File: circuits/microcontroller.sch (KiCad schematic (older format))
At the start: 18 parts, among them J2 Conn_02x07_Odd_Even, SW2 SW_PUSH, SW3 SW_PUSH, SW4 SW_PUSH, U3 ESP-WROOM-32, U4 SI7020-A20

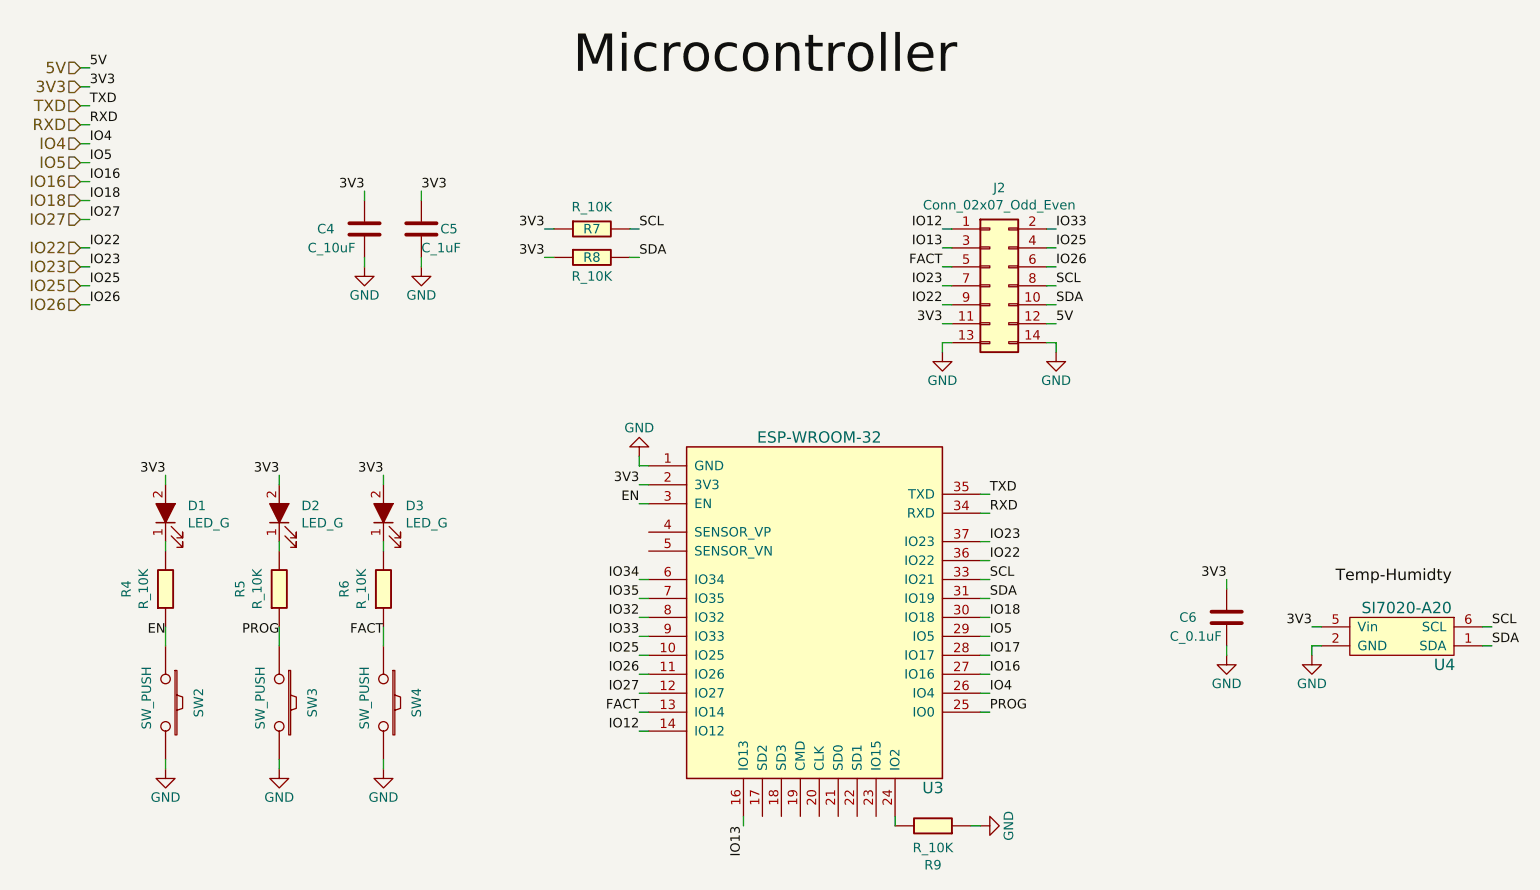
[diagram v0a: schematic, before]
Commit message: sending new board to boardhouse
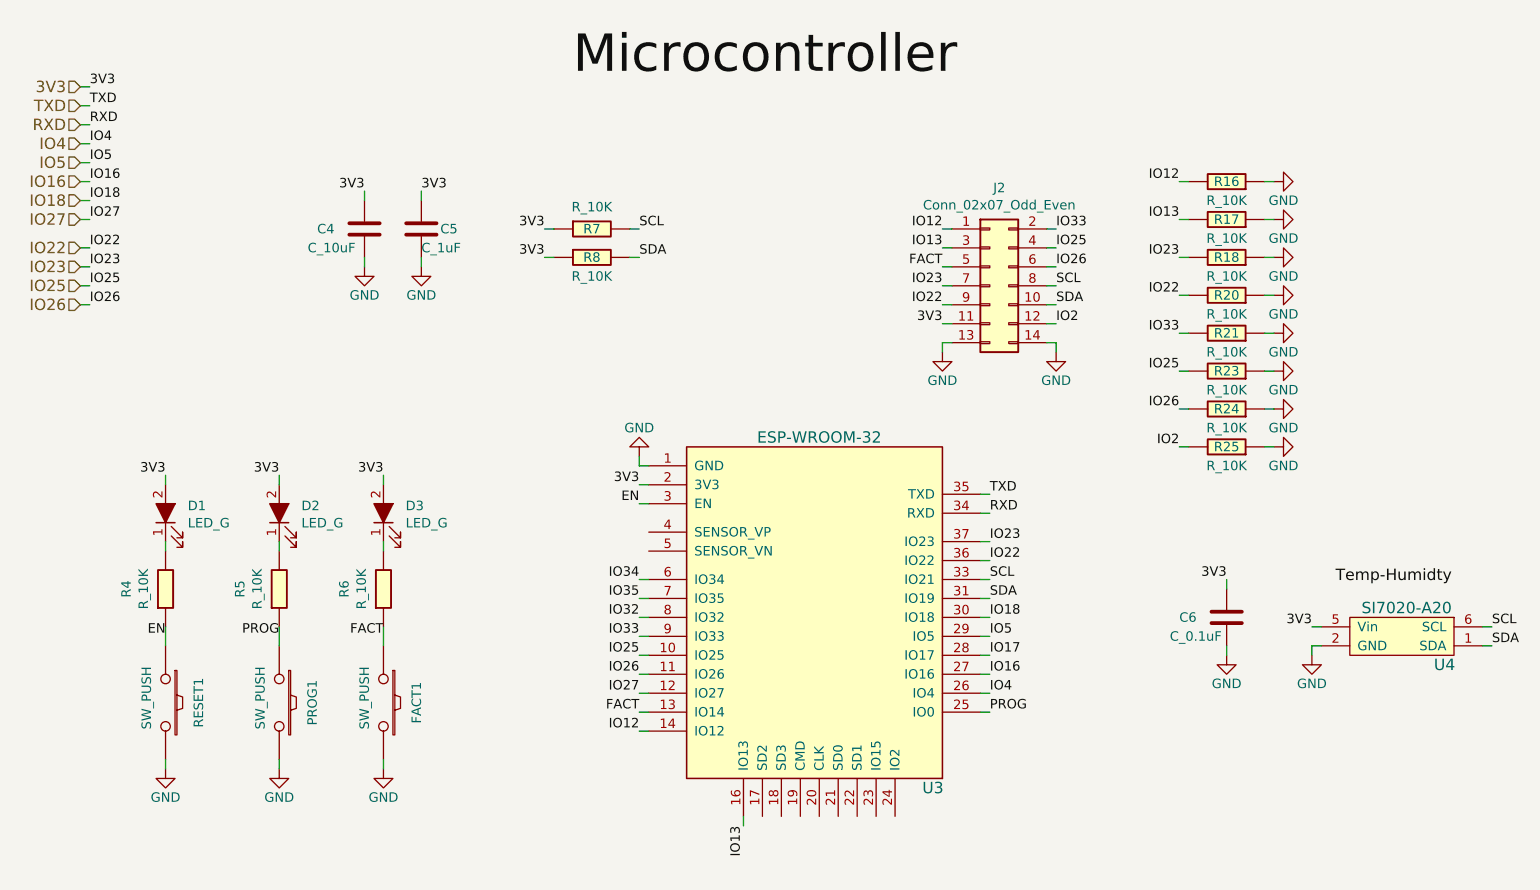
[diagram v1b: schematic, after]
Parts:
- removed R9: R_10K, Resistor_SMD:R_0603_1608Metric_Pad1.05x0.95mm_HandSolder, symbol led-controller-rescue:R_10K-open-automation
- added R16, R17, R18, R20, R21, R23, R24, R25: R_10K, Resistor_SMD:R_0603_1608Metric_Pad1.05x0.95mm_HandSolder, symbol led-controller-rescue:R_10K-open-automation
- renumbered SW4 to FACT1, SW3 to PROG1, SW2 to RESET1
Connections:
- net GND: now also R16.1, R17.1, R18.1, R20.1, R21.1, R23.1, R24.1, R25.1
- net IO12: now also R16.2
- net IO13: now also R17.2
- net IO22: now also R20.2
- net IO23: now also R18.2
- net IO25: now also R23.2
- net IO26: now also R24.2
- net IO33: now also R21.2
- net 5V renamed IO2
- net IO2: now also R25.2
